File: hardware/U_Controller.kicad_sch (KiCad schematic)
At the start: 16 parts, among them J7001 Conn_01x06_Pin, J7002 Conn_ARM_JTAG_SWD_10, J7003 USB_C_Receptacle_USB2.0_16P, SW7001 SW_Wuerth_450301014042, U7002 STM32C071RBT6, U7003 USBLC6-2SC6, Y7001 Crystal_GND24

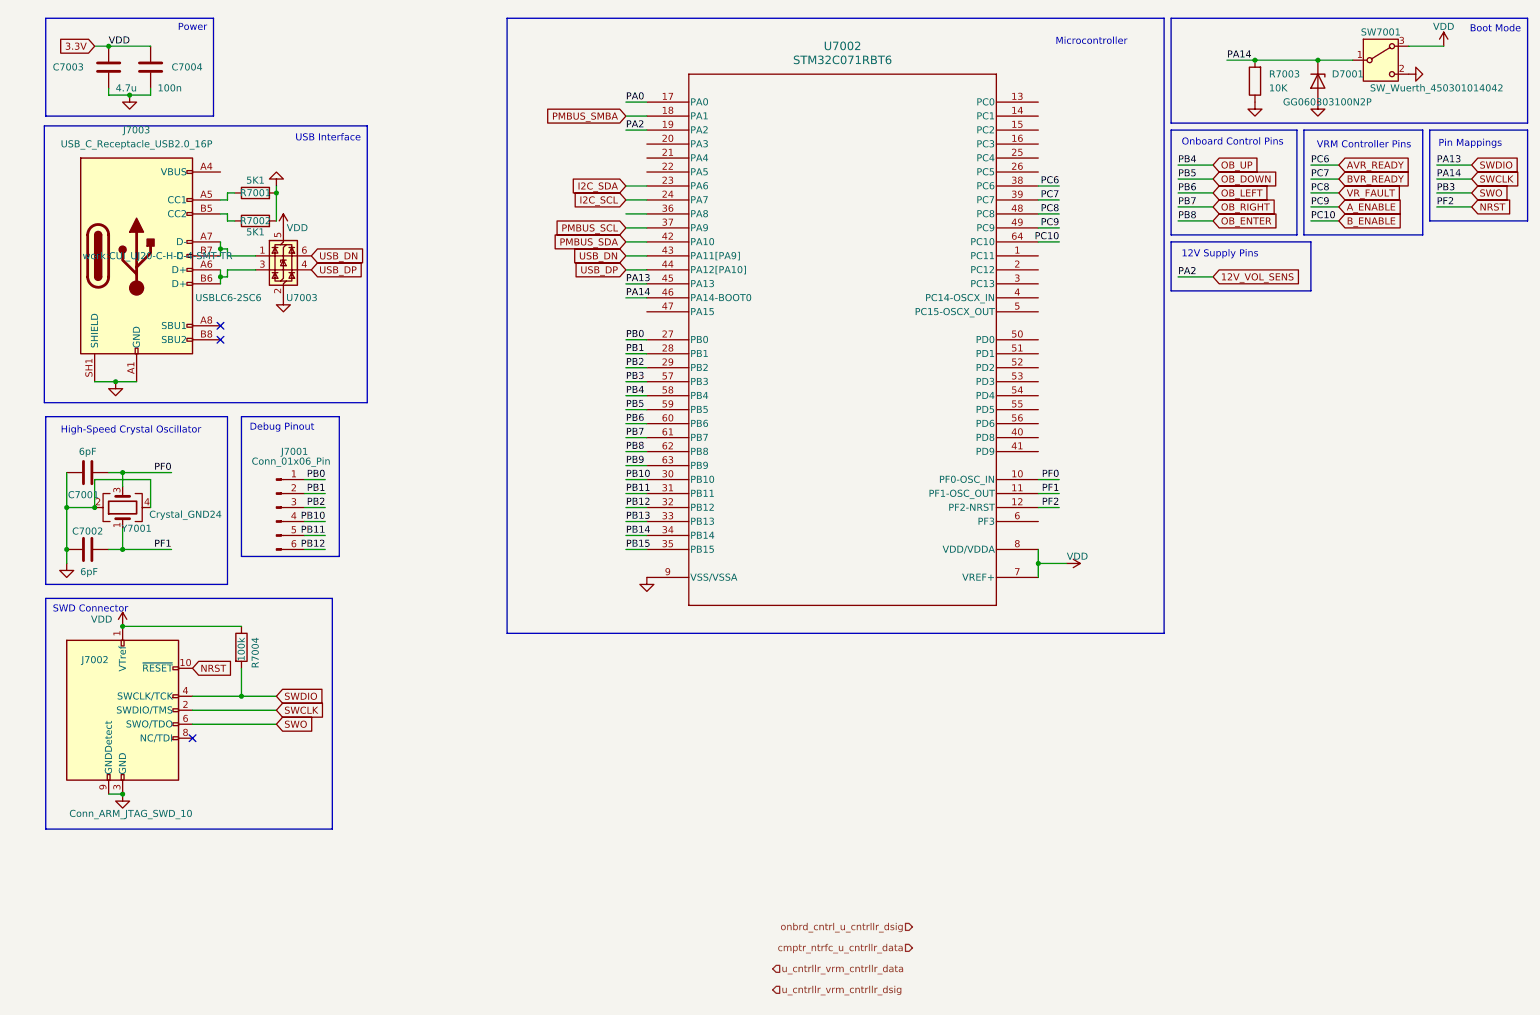
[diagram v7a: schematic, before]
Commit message: feat(schematic): migrate to stm32f401re
Migrates to the stm32f401re in the schematic and pin mappings (for the
most part)
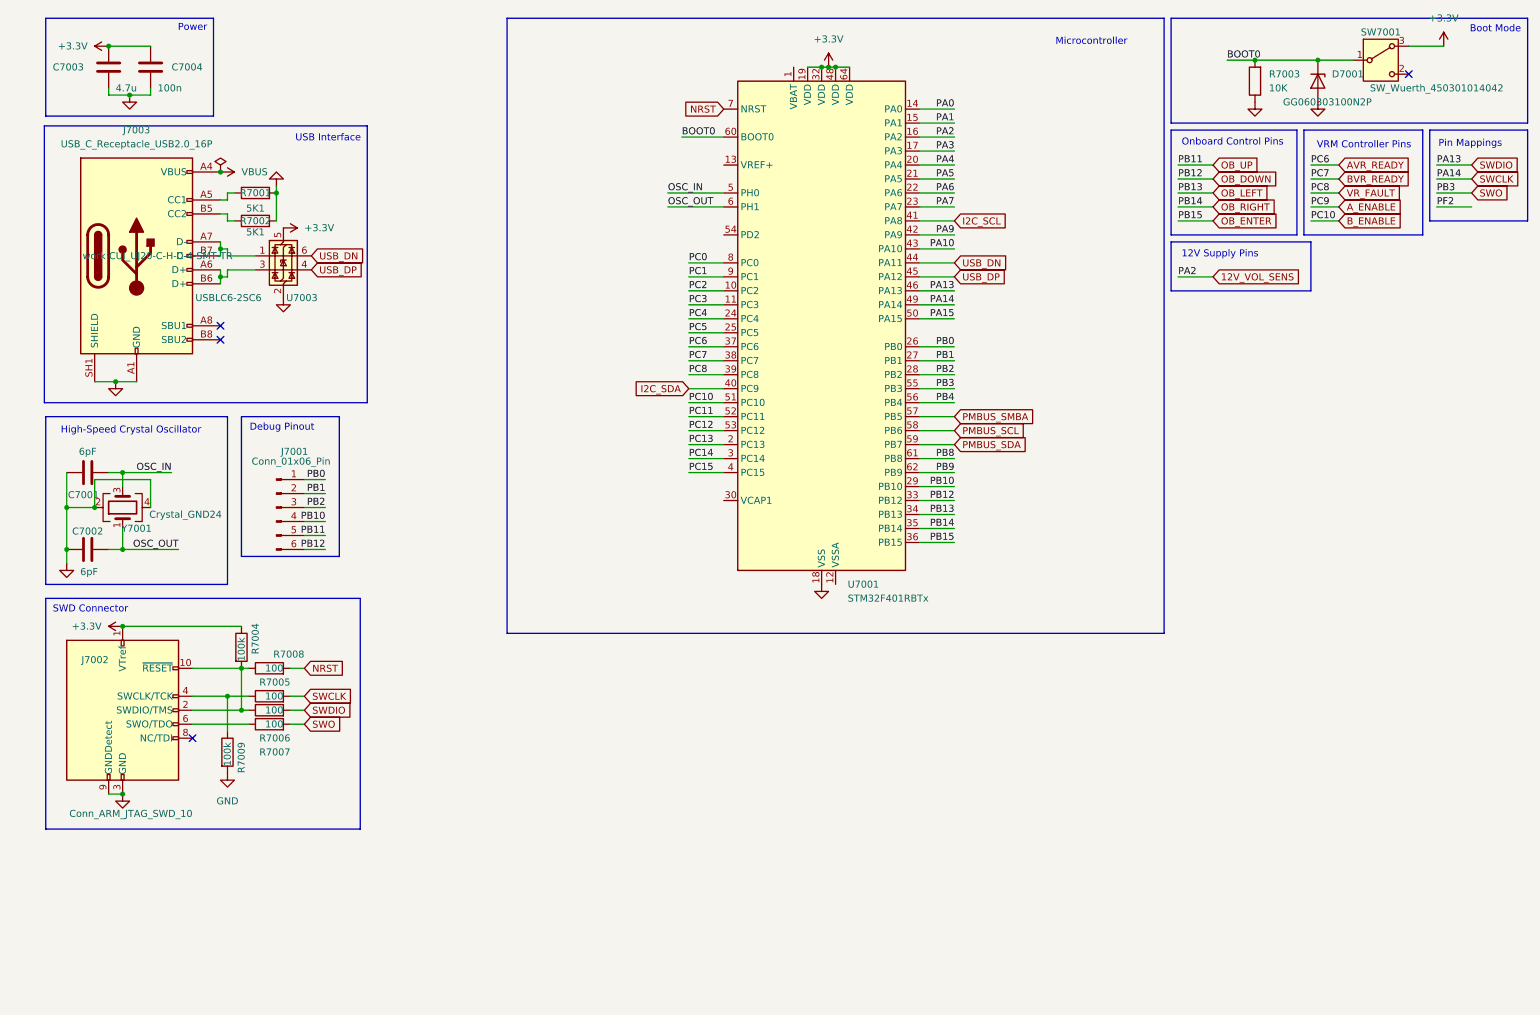
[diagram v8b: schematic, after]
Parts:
- removed U7002: STM32C071RBT6, work:LQFP-64_STM, symbol Symbol_Library:STM32C071RBT6
- added R7005, R7006, R7007, R7008: 100, Resistor_SMD:R_0805_2012Metric, symbol Device:R
- added R7009: 100k, Resistor_SMD:R_0805_2012Metric, symbol Device:R
- added U7001: STM32F401RBTx, Package_QFP:LQFP-64_10x10mm_P0.5mm, symbol MCU_ST_STM32F4:STM32F401RBTx
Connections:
- net PB11 is gone; now on net OB_UP: J7001.5 (Pin_5)
- net PB12 is gone; now on net OB_DOWN: J7001.6 (Pin_6)
- net 12V_VOL_SENS: now also U7001.16 (PA2)
- net AVR_READY: now also U7001.37 (PC6)
- net BVR_READY: now also U7001.38 (PC7)
- net B_ENABLE: now also U7001.51 (PC10)
- net GND: now also R7009.2, U7001.18 (VSS), U7001.31 (VSS), U7001.47 (VSS), U7001.63 (VSS); no longer SW7001.2 (C)
- net I2C_SCL: now also U7001.41 (PA8)
- net I2C_SDA: now also U7001.40 (PC9)
- net NRST: now also R7008.2, U7001.7 (NRST); no longer J7002.10 (~{RESET})
- net OB_DOWN: now also U7001.33 (PB12)
- net OB_ENTER: now also U7001.36 (PB15)
- net OB_LEFT: now also U7001.34 (PB13)
- net OB_RIGHT: now also U7001.35 (PB14)
- net PA0: now also U7001.14 (PA0)
- net PB0: now also U7001.26 (PB0)
- net PB1: now also U7001.27 (PB1)
- net PB10: now also U7001.29 (PB10)
- net PB2: now also U7001.28 (PB2)
- net PB9: now also U7001.62 (PB9)
- net PMBUS_SCL: now also U7001.58 (PB6)
- net PMBUS_SDA: now also U7001.59 (PB7)
- net PMBUS_SMBA: now also U7001.57 (PB5)
- net SWCLK: now also R7005.2, U7001.49 (PA14); no longer D7001.1 (K), J7002.2 (SWDIO/TMS), R7003.2, SW7001.1 (B)
- net SWDIO: now also R7006.2, U7001.46 (PA13); no longer J7002.4 (SWCLK/TCK), R7004.2
- net SWO: now also R7007.2, U7001.55 (PB3); no longer J7002.6 (SWO/TDO)
- net USB_DN: now also U7001.44 (PA11)
- net USB_DP: now also U7001.45 (PA12)
- net VR_FAULT: now also U7001.39 (PC8)
- net VBUS: now reaches J7003.A4 (VBUS), J7003.B4 (VBUS)
- net PF0 renamed OSC_IN
- net OSC_IN: now also U7001.5 (PH0)
- net PF1 renamed OSC_OUT
- net OSC_OUT: now also U7001.6 (PH1)
- net VDD renamed +3.3V
- net +3.3V: now also U7001.19 (VDD), U7001.32 (VDD), U7001.48 (VDD), U7001.64 (VDD)
- new net: J7002.6 (SWO/TDO), R7007.1
- new net: J7002.4 (SWCLK/TCK), R7005.1, R7009.1
- new net: J7002.10 (~{RESET}), J7002.2 (SWDIO/TMS), R7004.2, R7006.1, R7008.1
- new net BOOT0: D7001.1 (K), R7003.2, SW7001.1 (B), U7001.60 (BOOT0)
- new net PA1: U7001.15 (PA1)
- new net PA10: U7001.43 (PA10)
- new net PA15: U7001.50 (PA15)
- new net PA3: U7001.17 (PA3)
- new net PA4: U7001.20 (PA4)
- new net PA5: U7001.21 (PA5)
- new net PA6: U7001.22 (PA6)
- new net PA7: U7001.23 (PA7)
- new net PA9: U7001.42 (PA9)
- new net PB4: U7001.56 (PB4)
- new net PB8: U7001.61 (PB8)
- new net PC0: U7001.8 (PC0)
- new net PC1: U7001.9 (PC1)
- new net PC11: U7001.52 (PC11)
- new net PC12: U7001.53 (PC12)
- new net PC13: U7001.2 (PC13)
- new net PC14: U7001.3 (PC14)
- new net PC15: U7001.4 (PC15)
- new net PC2: U7001.10 (PC2)
- new net PC3: U7001.11 (PC3)
- new net PC4: U7001.24 (PC4)
- new net PC5: U7001.25 (PC5)
- no-connect marks 3 -> 4
